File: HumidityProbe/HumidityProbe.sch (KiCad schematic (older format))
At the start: 9 parts

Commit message: added 7 pins connector for BME sensors
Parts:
- added J?: Conn_01x07_Female, symbol Connector:Conn_01x07_Female
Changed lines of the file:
@@
 Text Label 7550 2900 0    50   ~ 0
 SDA
+$Comp
+L Connector:Conn_01x07_Female J?
+U 1 1 5FD0A4CF
+P 4450 6300
+F 0 "J?" H 4478 6326 50  0000 L CNN
+F 1 "Conn_01x07_Female" H 4478 6235 50  0000 L CNN
+F 2 "" H 4450 6300 50  0001 C CNN
+F 3 "~" H 4450 6300 50  0001 C CNN
+	1    4450 6300
+	1    0    0    -1
+$EndComp
 $EndSCHEMATC

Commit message: added lables to connectors
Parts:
- J?: value Conn_01x08_Female -> SSD1306 Connector
- J?: value Conn_01x03_Female -> Soil Sensor Connector
- J?: value Conn_01x03_Female -> Motion Sensor Connector
- J?: value Conn_01x07_Female -> BME 280 Connector
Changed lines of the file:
@@
 P 5450 5050
 F 0 "J?" H 5478 5026 50  0000 L CNN
-F 1 "Conn_01x08_Female" H 5478 4935 50  0000 L CNN
+F 1 "SSD1306 Connector" H 5478 4935 50  0000 L CNN
 F 2 "" H 5450 5050 50  0001 C CNN
 F 3 "~" H 5450 5050 50  0001 C CNN
@@
 P 4400 5150
 F 0 "J?" H 4428 5176 50  0000 L CNN
-F 1 "Conn_01x03_Female" H 4428 5085 50  0000 L CNN
+F 1 "Soil Sensor Connector" H 4428 5085 50  0000 L CNN
 F 2 "" H 4400 5150 50  0001 C CNN
 F 3 "~" H 4400 5150 50  0001 C CNN
@@
 P 7500 5150
 F 0 "J?" H 7528 5176 50  0000 L CNN
-F 1 "Conn_01x03_Female" H 7528 5085 50  0000 L CNN
+F 1 "Motion Sensor Connector" H 7528 5085 50  0000 L CNN
 F 2 "" H 7500 5150 50  0001 C CNN
 F 3 "~" H 7500 5150 50  0001 C CNN
@@
 P 4450 6300
 F 0 "J?" H 4478 6326 50  0000 L CNN
-F 1 "Conn_01x07_Female" H 4478 6235 50  0000 L CNN
+F 1 "BME 280 Connector" H 4478 6235 50  0000 L CNN
 F 2 "" H 4450 6300 50  0001 C CNN
 F 3 "~" H 4450 6300 50  0001 C CNN

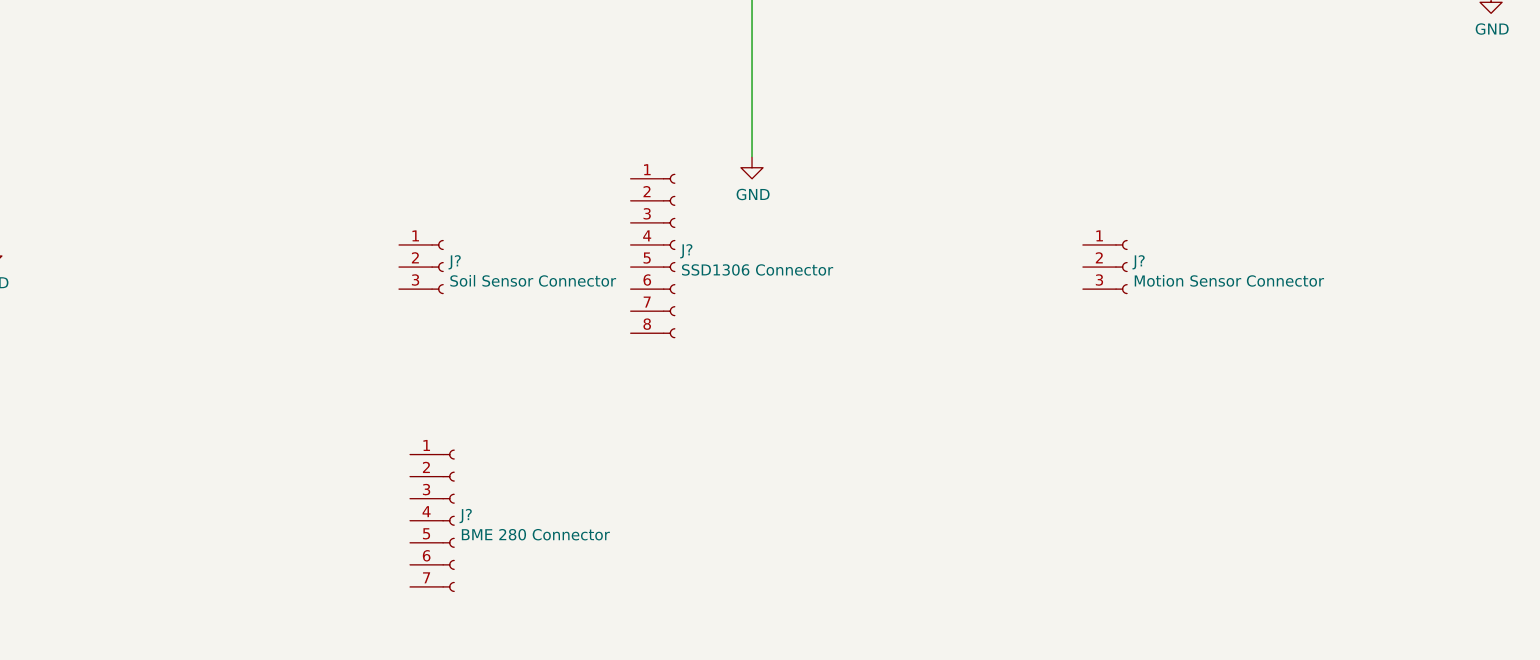
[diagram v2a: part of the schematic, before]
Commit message: added BME breakout footprint
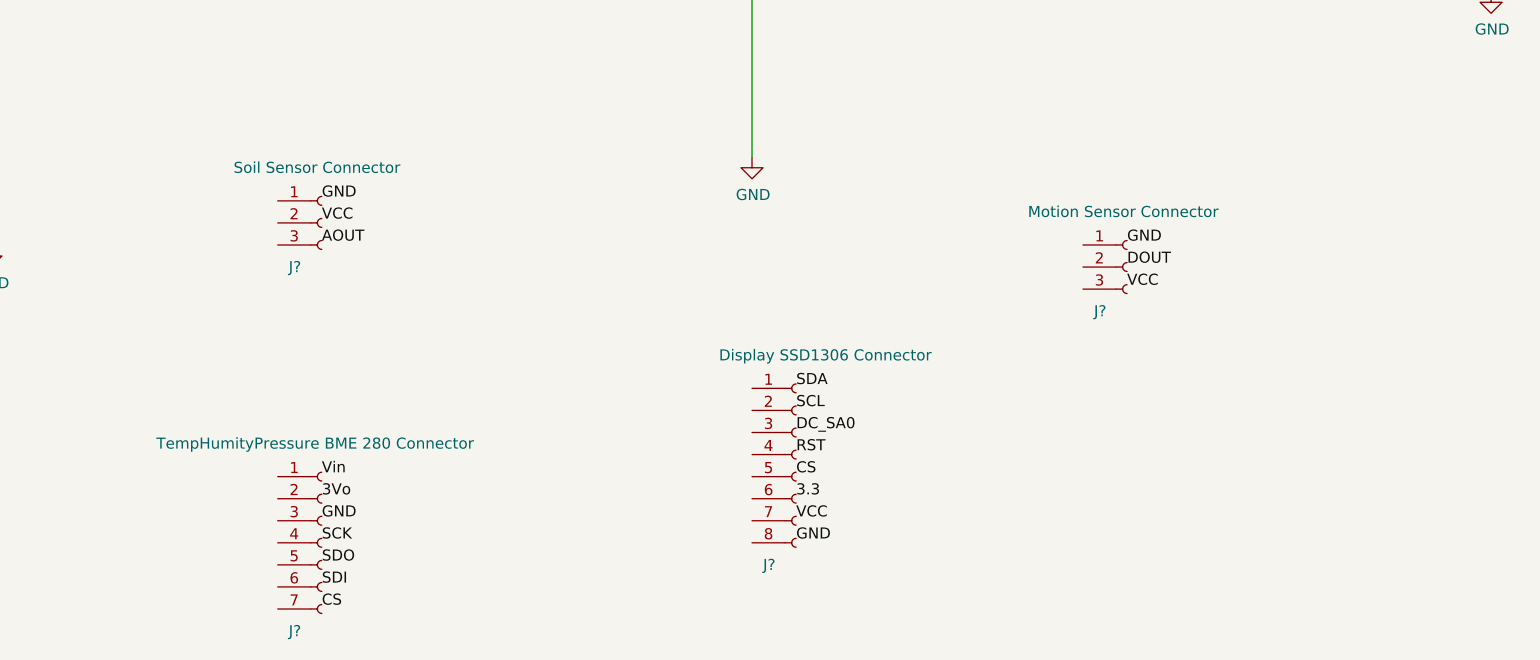
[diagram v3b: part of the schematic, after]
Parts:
- J?: value SSD1306 Connector -> Display SSD1306 Connector; footprint (none) -> Display:Adafruit_SSD1306
- J? (x2): footprint (none) -> Connector_PinHeader_1.27mm:PinHeader_1x03_P1.27mm_Horizontal
- J?: value BME 280 Connector -> TempHumityPressure BME 280 Connector; footprint (none) -> Display:Adafruit_BME280
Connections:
- net labels added: 3.3, 3Vo, AOUT, CS, DC_SA0, DOUT, RST, SCK, SDI, SDO, VCC, Vin
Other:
- moved on the sheet: J?
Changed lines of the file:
@@
 $EndDescr
-$Comp
-L Connector:Conn_01x08_Female J?
-U 1 1 5FA8EEEB
-P 5450 5050
-F 0 "J?" H 5478 5026 50  0000 L CNN
-F 1 "SSD1306 Connector" H 5478 4935 50  0000 L CNN
-F 2 "" H 5450 5050 50  0001 C CNN
-F 3 "~" H 5450 5050 50  0001 C CNN
-	1    5450 5050
-	1    0    0    -1
-$EndComp
 $Comp
 L power:+3.3V #PWR?
@@
 F 1 "BME280" H 3421 2755 50  0000 R CNN
 F 2 "Package_LGA:Bosch_LGA-8_2.5x2.5mm_P0.65mm_ClockwisePinNumbering" H 3850 2600 50  0001 C CNN
-F 3 "https://ae-bst.resource.bosch.com/media/_tech/media/datasheets/BST-BME280_DS001-11.pdf" H 3850 2600 50  0001 C CNN
+F 3 "${KIPRJMOD}/Docs/BST-BME280_DS001-10.pdf" H 3850 2600 50  0001 C CNN
 	1    3850 2800
 	1    0    0    -1
@@
 L Connector:Conn_01x03_Female J?
 U 1 1 5FA99197
-P 4400 5150
-F 0 "J?" H 4428 5176 50  0000 L CNN
-F 1 "Soil Sensor Connector" H 4428 5085 50  0000 L CNN
-F 2 "" H 4400 5150 50  0001 C CNN
-F 3 "~" H 4400 5150 50  0001 C CNN
-	1    4400 5150
+P 3850 4950
+F 0 "J?" H 3700 4750 50  0000 L CNN
+F 1 "Soil Sensor Connector" H 3450 5200 50  0000 L CNN
+F 2 "Connector_PinHeader_1.27mm:PinHeader_1x03_P1.27mm_Horizontal" H 3850 4950 50  0001 C CNN
+F 3 "~" H 3850 4950 50  0001 C CNN
+	1    3850 4950
 	1    0    0    -1
 $EndComp
@@
 U 1 1 5FAAEF1A
 P 7500 5150
-F 0 "J?" H 7528 5176 50  0000 L CNN
-F 1 "Motion Sensor Connector" H 7528 5085 50  0000 L CNN
-F 2 "" H 7500 5150 50  0001 C CNN
-F 3 "~" H 7500 5150 50  0001 C CNN
+F 0 "J?" H 7350 4950 50  0000 L CNN
+F 1 "Motion Sensor Connector" H 7050 5400 50  0000 L CNN
+F 2 "Connector_PinHeader_1.27mm:PinHeader_1x03_P1.27mm_Horizontal" H 7500 5150 50  0001 C CNN
+F 3 "${KIPRJMOD}/Docs/pir-passive-infrared-proximity-motion-sensor.pdf" H 7500 5150 50  0001 C CNN
 	1    7500 5150
 	1    0    0    -1
@@
 F 1 "Photon" H 7000 2047 60  0000 C CNN
 F 2 "ParticleFP:photon_tht" H 7000 1941 60  0000 C CNN
-F 3 "" H 7500 3850 60  0000 C CNN
+F 3 "${KIPRJMOD}/Docs/photon-datasheet.pdf" H 7500 3850 60  0001 C CNN
 	1    6950 2800
 	1    0    0    -1
@@
 L Connector:Conn_01x07_Female J?
 U 1 1 5FD0A4CF
-P 4450 6300
-F 0 "J?" H 4478 6326 50  0000 L CNN
-F 1 "BME 280 Connector" H 4478 6235 50  0000 L CNN
-F 2 "" H 4450 6300 50  0001 C CNN
-F 3 "~" H 4450 6300 50  0001 C CNN
-	1    4450 6300
-	1    0    0    -1
-$EndComp
+P 3850 6400
+F 0 "J?" H 3700 6000 50  0000 L CNN
+F 1 "TempHumityPressure BME 280 Connector" H 3100 6850 50  0000 L CNN
+F 2 "Display:Adafruit_BME280" H 3850 6400 50  0001 C CNN
+F 3 "${KIPRJMOD}/Docs/BST-BME280_DS001-10.pdf" H 3850 6400 50  0001 C CNN
+	1    3850 6400
+	1    0    0    -1
+$EndComp
+Text Label 3850 6100 0    50   ~ 0
+Vin
+Text Label 3850 6200 0    50   ~ 0
+3Vo
+Text Label 3850 6300 0    50   ~ 0
+GND
+Text Label 3850 6400 0    50   ~ 0
+SCK
+Text Label 3850 6500 0    50   ~ 0
+SDO
+Text Label 3850 6600 0    50   ~ 0
+SDI
+Text Label 3850 6700 0    50   ~ 0
+CS
+Text Label 6000 5700 0    50   ~ 0
+SDA
+Text Label 6000 5800 0    50   ~ 0
+SCL
+Text Label 6000 5900 0    50   ~ 0
+DC_SA0
+Text Label 6000 6000 0    50   ~ 0
+RST
+Text Label 6000 6100 0    50   ~ 0
+CS
+Text Label 6000 6200 0    50   ~ 0
+3.3
+Text Label 6000 6300 0    50   ~ 0
+VCC
+Text Label 6000 6400 0    50   ~ 0
+GND
+Text Label 3850 4850 0    50   ~ 0
+GND
+Text Label 3850 4950 0    50   ~ 0
+VCC
+Text Label 3850 5050 0    50   ~ 0
+AOUT
+Text Label 7500 5250 0    50   ~ 0
+VCC
+Text Label 7500 5050 0    50   ~ 0
+GND
+Text Label 7500 5150 0    50   ~ 0
+DOUT
+$Comp
+L Connector:Conn_01x08_Female J?
+U 1 1 5FA8EEEB
+P 6000 6000
+F 0 "J?" H 5850 5500 50  0000 L CNN
+F 1 "Display SSD1306 Connector" H 5650 6450 50  0000 L CNN
+F 2 "Display:Adafruit_SSD1306" H 6000 6000 50  0001 C CNN
+F 3 "${KIPRJMOD}/Docs/SSD1306.pdf" H 6000 6000 50  0001 C CNN
+	1    6000 6000
+	1    0    0    -1
+$EndComp

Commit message: moved BME280 to project local library
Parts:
- J?: footprint Display:Adafruit_BME280 -> Adafruit_BME280:Adafruit_BME280
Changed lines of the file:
@@
 F 0 "J?" H 3700 6000 50  0000 L CNN
 F 1 "TempHumityPressure BME 280 Connector" H 3100 6850 50  0000 L CNN
-F 2 "Display:Adafruit_BME280" H 3850 6400 50  0001 C CNN
+F 2 "Adafruit_BME280:Adafruit_BME280" H 3850 6400 50  0001 C CNN
 F 3 "${KIPRJMOD}/Docs/BST-BME280_DS001-10.pdf" H 3850 6400 50  0001 C CNN
 	1    3850 6400

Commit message: some connections
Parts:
- removed U?: BME280, Package_LGA:Bosch_LGA-8_2.5x2.5mm_P0.65mm_ClockwisePinNumbering, symbol Sensor:BME280
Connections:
- wire segments 23 -> 51
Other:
- moved on the sheet: D?, J?, R?, U?

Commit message: added usb power connector
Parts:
- added J?: USB_B_Micro, symbol Connector:USB_B_Micro
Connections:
- wire segments 51 -> 55
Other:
- moved on the sheet: D?, R?
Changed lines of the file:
@@
 $EndComp
 Wire Wire Line
-	5950 4000 5950 4250
-Wire Wire Line
-	5950 5150 5950 5450
+	5300 5000 5300 5300
 $Comp
 L power:GND #PWR?
 U 1 1 5FABAED4
-P 5950 5450
-F 0 "#PWR?" H 5950 5200 50  0001 C CNN
-F 1 "GND" H 5955 5277 50  0000 C CNN
-F 2 "" H 5950 5450 50  0001 C CNN
-F 3 "" H 5950 5450 50  0001 C CNN
-	1    5950 5450
-	1    0    0    -1
-$EndComp
-$Comp
-L power:GND #PWR?
-U 1 1 5FA9263D
-P 3150 5100
-F 0 "#PWR?" H 3150 4850 50  0001 C CNN
-F 1 "GND" H 3155 4927 50  0000 C CNN
-F 2 "" H 3150 5100 50  0001 C CNN
-F 3 "" H 3150 5100 50  0001 C CNN
-	1    3150 5100
-	1    0    0    -1
-$EndComp
-Wire Wire Line
-	3150 3150 3150 5100
-Wire Wire Line
-	5950 4550 5950 4850
+P 5300 5300
+F 0 "#PWR?" H 5300 5050 50  0001 C CNN
+F 1 "GND" H 5305 5127 50  0000 C CNN
+F 2 "" H 5300 5300 50  0001 C CNN
+F 3 "" H 5300 5300 50  0001 C CNN
+	1    5300 5300
+	1    0    0    -1
+$EndComp
+Wire Wire Line
+	5300 4400 5300 4700
 $Comp
 L Device:LED D?
 U 1 1 5FAB79FC
-P 5950 5000
-F 0 "D?" V 5989 4883 50  0000 R CNN
-F 1 "LED" V 5898 4883 50  0000 R CNN
-F 2 "" H 5950 5000 50  0001 C CNN
-F 3 "~" H 5950 5000 50  0001 C CNN
-	1    5950 5000
+P 5300 4850
+F 0 "D?" V 5339 4733 50  0000 R CNN
+F 1 "LED" V 5248 4733 50  0000 R CNN
+F 2 "" H 5300 4850 50  0001 C CNN
+F 3 "~" H 5300 4850 50  0001 C CNN
+	1    5300 4850
 	0    -1   -1   0
 $EndComp
@@
 L Device:R_US R?
 U 1 1 5FAB661E
-P 5950 4400
-F 0 "R?" H 6018 4446 50  0000 L CNN
-F 1 "R_US" H 6018 4355 50  0000 L CNN
-F 2 "" V 5990 4390 50  0001 C CNN
-F 3 "~" H 5950 4400 50  0001 C CNN
-	1    5950 4400
-	1    0    0    -1
-$EndComp
-Wire Wire Line
-	3350 3050 3550 3050
-Wire Wire Line
-	4300 1950 4300 2050
+P 5300 4250
+F 0 "R?" H 5368 4296 50  0000 L CNN
+F 1 "R_US" H 5368 4205 50  0000 L CNN
+F 2 "" V 5340 4240 50  0001 C CNN
+F 3 "~" H 5300 4250 50  0001 C CNN
+	1    5300 4250
+	1    0    0    -1
+$EndComp
+Wire Wire Line
+	5100 3350 6900 3350
+Wire Wire Line
+	6900 3350 6900 2350
+Wire Wire Line
+	6900 2350 8400 2350
+Connection ~ 5100 3350
+Wire Wire Line
+	6900 3350 6900 4250
+Wire Wire Line
+	6900 4250 8400 4250
+Connection ~ 6900 3350
+Wire Wire Line
+	8400 4150 8200 4150
+Wire Wire Line
+	8200 4150 8200 4400
+Wire Wire Line
+	8400 4050 7100 4050
+Wire Wire Line
+	7100 4050 7100 3450
+Wire Wire Line
+	7100 3450 5650 3450
+Connection ~ 5650 3450
+Wire Wire Line
+	8400 2450 7100 2450
+Wire Wire Line
+	7100 2450 7100 3450
+Connection ~ 7100 3450
+Wire Wire Line
+	8200 4150 8200 3950
+Wire Wire Line
+	8200 3950 8400 3950
+Connection ~ 8200 4150
+$Comp
+L power:GND #PWR?
+U 1 1 5FD63FB3
+P 8250 3150
+F 0 "#PWR?" H 8250 2900 50  0001 C CNN
+F 1 "GND" H 8255 2977 50  0000 C CNN
+F 2 "" H 8250 3150 50  0001 C CNN
+F 3 "" H 8250 3150 50  0001 C CNN
+	1    8250 3150
+	1    0    0    -1
+$EndComp
+Wire Wire Line
+	8400 3050 8250 3050
+Wire Wire Line
+	8250 3050 8250 3150
+$Comp
+L power:+3.3V #PWR?
+U 1 1 5FD685A5
+P 8050 3250
+F 0 "#PWR?" H 8050 3100 50  0001 C CNN
+F 1 "+3.3V" H 8065 3423 50  0000 C CNN
+F 2 "" H 8050 3250 50  0001 C CNN
+F 3 "" H 8050 3250 50  0001 C CNN
+	1    8050 3250
+	1    0    0    -1
+$EndComp
+Wire Wire Line
+	8050 3250 8050 3500
+$Comp
+L power:GND #PWR?
+U 1 1 5FD69BA6
+P 4300 4400
+F 0 "#PWR?" H 4300 4150 50  0001 C CNN
+F 1 "GND" H 4305 4227 50  0000 C CNN
+F 2 "" H 4300 4400 50  0001 C CNN
+F 3 "" H 4300 4400 50  0001 C CNN
+	1    4300 4400
+	1    0    0    -1
+$EndComp
+Wire Wire Line
+	4250 3800 4250 4350
+Wire Wire Line
+	4250 4350 4300 4350
+Connection ~ 4300 4350
+Wire Wire Line
+	4300 4350 4300 4400
+Wire Wire Line
+	4400 3800 4400 4350
+Wire Wire Line
+	4400 4350 4300 4350
+Wire Wire Line
+	4300 2050 4400 2050
+Wire Wire Line
+	4400 2050 4400 2150
+Wire Wire Line
+	4300 2050 4300 2150
+$Comp
+L power:+3.3V #PWR?
+U 1 1 5FD727D7
+P 6950 4700
+F 0 "#PWR?" H 6950 4550 50  0001 C CNN
+F 1 "+3.3V" H 6965 4873 50  0000 C CNN
+F 2 "" H 6950 4700 50  0001 C CNN
+F 3 "" H 6950 4700 50  0001 C CNN
+	1    6950 4700
+	1    0    0    -1
+$EndComp
+Wire Wire Line
+	7300 5250 6950 5250
+Wire Wire Line
+	6950 4700 6950 5250
+Wire Wire Line
+	7300 5900 6950 5900
+Wire Wire Line
+	6950 5900 6950 5250
+Connection ~ 6950 5250
+Wire Wire Line
+	7300 5050 7100 5050
+Wire Wire Line
+	7100 5050 7100 5800
+Connection ~ 7100 5800
+Wire Wire Line
+	7100 5800 7300 5800
+$Comp
+L power:GND #PWR?
+U 1 1 5FD758BE
+P 7100 6150
+F 0 "#PWR?" H 7100 5900 50  0001 C CNN
+F 1 "GND" H 7105 5977 50  0000 C CNN
+F 2 "" H 7100 6150 50  0001 C CNN
+F 3 "" H 7100 6150 50  0001 C CNN
+	1    7100 6150
+	1    0    0    -1
+$EndComp
+Wire Wire Line
+	7100 5800 7100 6150
+Wire Wire Line
+	7300 6000 3500 6000
+Wire Wire Line
+	3500 6000 3500 3450
+Wire Wire Line
+	3500 3450 3850 3450
+Wire Wire Line
+	7300 5150 6550 5150
+Wire Wire Line
+	6550 5150 6550 3250
+Wire Wire Line
+	6550 3250 4850 3250
+$Comp
+L Connector:USB_B_Micro J?
+U 1 1 5FD80103
+P 2050 2200
+F 0 "J?" H 2107 2667 50  0000 C CNN
+F 1 "USB_B_Micro" H 2107 2576 50  0000 C CNN
+F 2 "" H 2200 2150 50  0001 C CNN
+F 3 "~" H 2200 2150 50  0001 C CNN
+	1    2050 2200
+	1    0    0    -1
+$EndComp
+Connection ~ 4300 2050
 $Comp
 L power:+3.3V #PWR?
@@
 $EndComp
 Wire Wire Line
-	3550 3150 3150 3150
-Wire Wire Line
-	5100 3350 6900 3350
-Wire Wire Line
-	6900 3350 6900 2350
-Wire Wire Line
-	6900 2350 8400 2350
-Connection ~ 5100 3350
-Wire Wire Line
-	6900 3350 6900 4250
-Wire Wire Line
-	6900 4250 8400 4250
-Connection ~ 6900 3350
-Wire Wire Line
-	8400 4150 8200 4150
-Wire Wire Line
-	8200 4150 8200 4400
-Wire Wire Line
-	8400 4050 7100 4050
-Wire Wire Line
-	7100 4050 7100 3450
-Wire Wire Line
-	7100 3450 5650 3450
-Connection ~ 5650 3450
-Wire Wire Line
-	8400 2450 7100 2450
-Wire Wire Line
-	7100 2450 7100 3450
-Connection ~ 7100 3450
-Wire Wire Line
-	8200 4150 8200 3950
-Wire Wire Line
-	8200 3950 8400 3950
-Connection ~ 8200 4150
-$Comp
-L power:GND #PWR?
-U 1 1 5FD63FB3
-P 8250 3150
-F 0 "#PWR?" H 8250 2900 50  0001 C CNN
-F 1 "GND" H 8255 2977 50  0000 C CNN
-F 2 "" H 8250 3150 50  0001 C CNN
-F 3 "" H 8250 3150 50  0001 C CNN
-	1    8250 3150
-	1    0    0    -1
-$EndComp
-Wire Wire Line
-	8400 3050 8250 3050
-Wire Wire Line
-	8250 3050 8250 3150
-$Comp
-L power:+3.3V #PWR?
-U 1 1 5FD685A5
-P 8050 3250
-F 0 "#PWR?" H 8050 3100 50  0001 C CNN
-F 1 "+3.3V" H 8065 3423 50  0000 C CNN
-F 2 "" H 8050 3250 50  0001 C CNN
-F 3 "" H 8050 3250 50  0001 C CNN
-	1    8050 3250
-	1    0    0    -1
-$EndComp
-Wire Wire Line
-	8050 3250 8050 3500
-$Comp
-L power:GND #PWR?
-U 1 1 5FD69BA6
-P 4300 4400
-F 0 "#PWR?" H 4300 4150 50  0001 C CNN
-F 1 "GND" H 4305 4227 50  0000 C CNN
-F 2 "" H 4300 4400 50  0001 C CNN
-F 3 "" H 4300 4400 50  0001 C CNN
-	1    4300 4400
-	1    0    0    -1
-$EndComp
-Wire Wire Line
-	4250 3800 4250 4350
-Wire Wire Line
-	4250 4350 4300 4350
-Connection ~ 4300 4350
-Wire Wire Line
-	4300 4350 4300 4400
-Wire Wire Line
-	4400 3800 4400 4350
-Wire Wire Line
-	4400 4350 4300 4350
-Wire Wire Line
-	4300 2050 4400 2050
-Wire Wire Line
-	4400 2050 4400 2150
-Connection ~ 4300 2050
-Wire Wire Line
-	4300 2050 4300 2150
-$Comp
-L power:+3.3V #PWR?
-U 1 1 5FD727D7
-P 6950 4700
-F 0 "#PWR?" H 6950 4550 50  0001 C CNN
-F 1 "+3.3V" H 6965 4873 50  0000 C CNN
-F 2 "" H 6950 4700 50  0001 C CNN
-F 3 "" H 6950 4700 50  0001 C CNN
-	1    6950 4700
-	1    0    0    -1
-$EndComp
-Wire Wire Line
-	7300 5250 6950 5250
-Wire Wire Line
-	6950 4700 6950 5250
-Wire Wire Line
-	7300 5900 6950 5900
-Wire Wire Line
-	6950 5900 6950 5250
-Connection ~ 6950 5250
-Wire Wire Line
-	7300 5050 7100 5050
-Wire Wire Line
-	7100 5050 7100 5800
-Connection ~ 7100 5800
-Wire Wire Line
-	7100 5800 7300 5800
-$Comp
-L power:GND #PWR?
-U 1 1 5FD758BE
-P 7100 6150
-F 0 "#PWR?" H 7100 5900 50  0001 C CNN
-F 1 "GND" H 7105 5977 50  0000 C CNN
-F 2 "" H 7100 6150 50  0001 C CNN
-F 3 "" H 7100 6150 50  0001 C CNN
-	1    7100 6150
-	1    0    0    -1
-$EndComp
-Wire Wire Line
-	7100 5800 7100 6150
-Wire Wire Line
-	7300 6000 3500 6000
-Wire Wire Line
-	3500 6000 3500 3450
-Wire Wire Line
-	3500 3450 3850 3450
-Wire Wire Line
-	7300 5150 6550 5150
-Wire Wire Line
-	6550 5150 6550 3250
-Wire Wire Line
-	6550 3250 4850 3250
+	4300 1950 4300 2050
+$Comp
+L power:+3.3V #PWR?
+U 1 1 5FD8261E
+P 2550 1950
+F 0 "#PWR?" H 2550 1800 50  0001 C CNN
+F 1 "+3.3V" H 2565 2123 50  0000 C CNN
+F 2 "" H 2550 1950 50  0001 C CNN
+F 3 "" H 2550 1950 50  0001 C CNN
+	1    2550 1950
+	1    0    0    -1
+$EndComp
+$Comp
+L power:GND #PWR?
+U 1 1 5FD83683
+P 2050 2800
+F 0 "#PWR?" H 2050 2550 50  0001 C CNN
+F 1 "GND" H 2055 2627 50  0000 C CNN
+F 2 "" H 2050 2800 50  0001 C CNN
+F 3 "" H 2050 2800 50  0001 C CNN
+	1    2050 2800
+	1    0    0    -1
+$EndComp
+Wire Wire Line
+	2350 2000 2550 2000
+Wire Wire Line
+	2550 2000 2550 1950
+Wire Wire Line
+	2050 2600 2050 2700
+Wire Wire Line
+	1950 2600 1950 2700
+Wire Wire Line
+	1950 2700 2050 2700
+Connection ~ 2050 2700
+Wire Wire Line
+	2050 2700 2050 2800
+Wire Wire Line
+	4850 3150 5300 3150
+Wire Wire Line
+	5300 3150 5300 4100
 $EndSCHEMATC

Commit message: added
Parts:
- added C? (x2): 200nF, Capacitor_THT:C_Disc_D8.0mm_W5.0mm_P7.50mm, symbol Device:C
- added C? (x2): 4.7uF, Capacitor_THT:C_Disc_D8.0mm_W5.0mm_P7.50mm, symbol Device:C
- added L?: 2.2uH, symbol pspice:INDUCTOR
- added R?: 10K, Resistor_THT:R_Axial_DIN0204_L3.6mm_D1.6mm_P7.62mm_Horizontal, symbol Device:R_US
- added R?: 15.8K, symbol Device:R_US
- added R?: 49.9K, symbol Device:R_US
- added R?: R_US, symbol Device:R_US
- added U?: BME280, Package_LGA:Bosch_LGA-8_2.5x2.5mm_P0.65mm_ClockwisePinNumbering, symbol Sensor:BME280
- added U?: AOZ1280CI, digikey-footprints:SOT-23-6, symbol dk_PMIC-Voltage-Regulators-DC-DC-Switching-Regulators:AOZ1280CI
- added Z?: 1N5231BTR, digikey-footprints:DO-35, symbol dk_Diodes-Zener-Single:1N5231BTR
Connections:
- net labels added: +5V
- wire segments 55 -> 91
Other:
- moved on the sheet: D?, J?, R?, U?
